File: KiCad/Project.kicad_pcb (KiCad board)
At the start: 2 copper layers, 70 x 40.6 mm, 46 parts, among them J2 Inputs Test Points, J3 Power & Output Test Points, Q1 BUK9832-55A, Q2 BUK9832-55A, SW1 Power, SW2 Fire, SW3 Freq Select, SW4 Fire Select, U1 TLV1117-50, U2 PIC16F1788-IP, U3 Audio Board

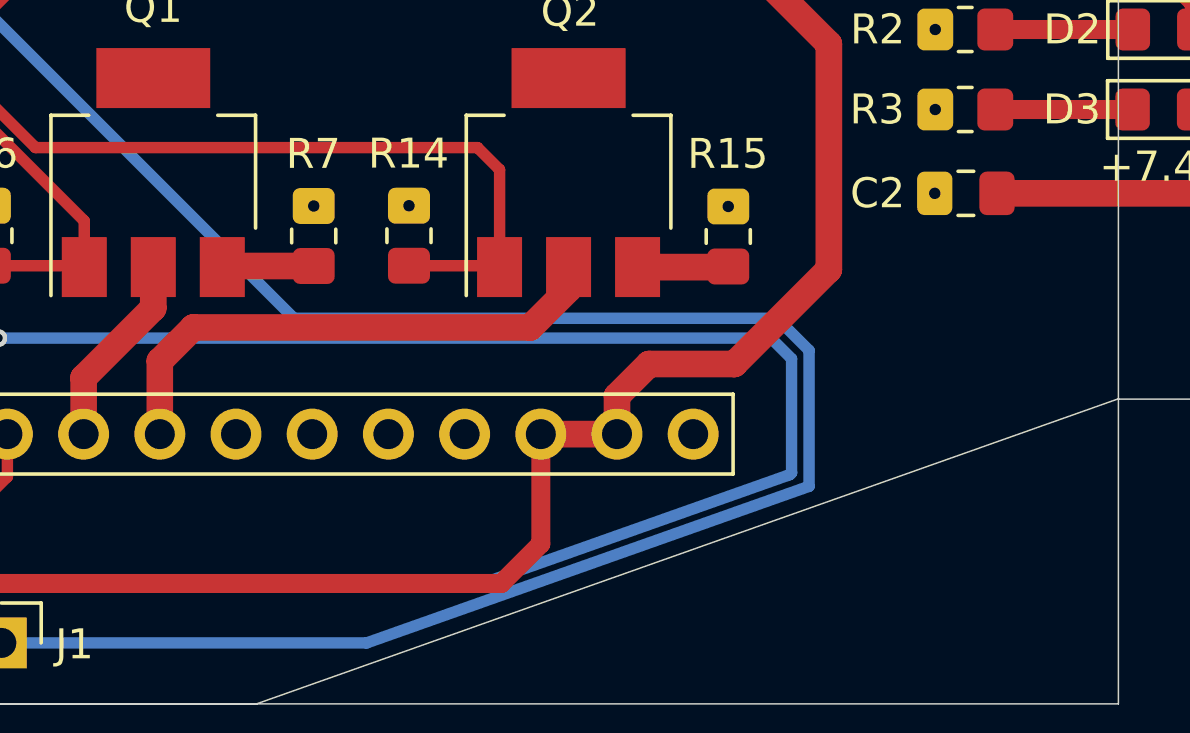
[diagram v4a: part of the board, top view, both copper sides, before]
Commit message: added title block and logo
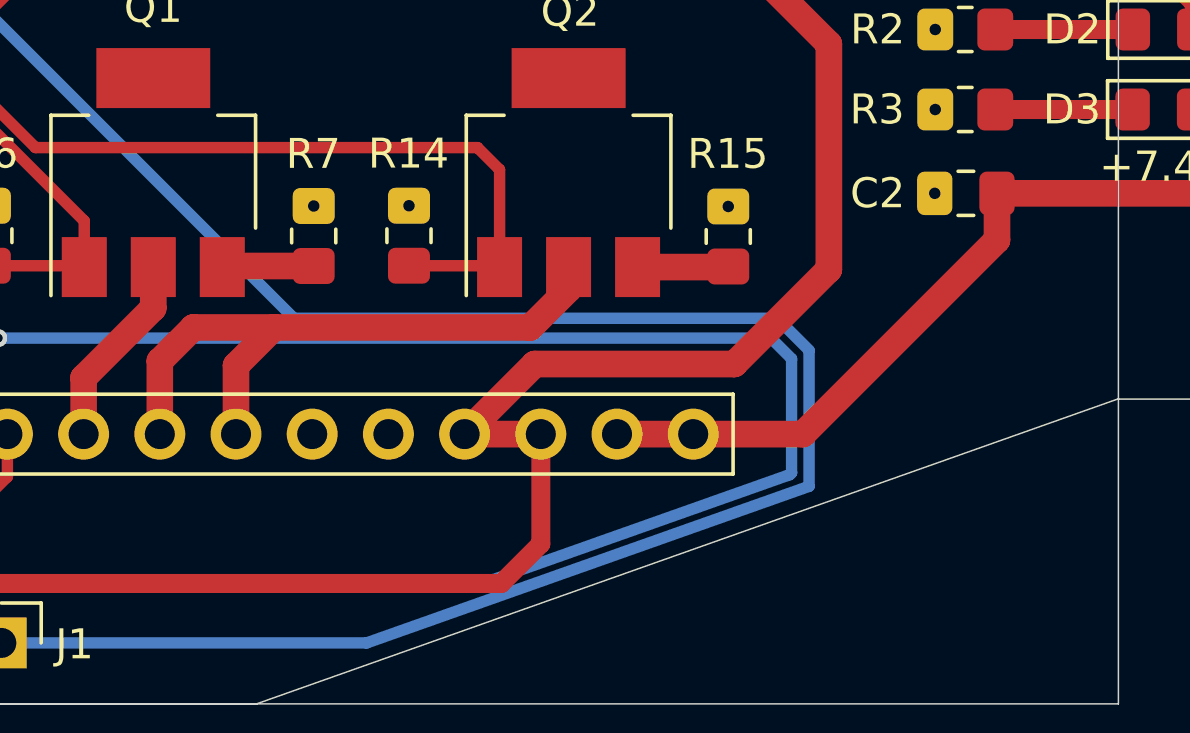
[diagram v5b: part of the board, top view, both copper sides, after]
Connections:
- REF** pad 10: (no net) -> GND
- REF** pad 12: GND -> +5V
- REF** pad 14: +5V -> Net-(D1-K)
- REF** pad 9: (no net) -> Net-(Q2-D)
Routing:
- net Net-(D1-K): track 77.0 -> 93.9 mm
- net +5V: track 143.8 -> 148.2 mm
- net Net-(Q2-D): track 22.4 -> 26.5 mm
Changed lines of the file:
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@@
 			(layers "*.Cu" "*.Mask")
 			(remove_unused_layers no)
+			(net 18 "Net-(Q2-D)")
 		)
 		(pad "10" thru_hole oval
@@
 			(layers "*.Cu" "*.Mask")
 			(remove_unused_layers no)
+			(net 2 "GND")
 		)
 		(pad "11" thru_hole oval
@@
 			(layers "*.Cu" "*.Mask")
 			(remove_unused_layers no)
-			(net 2 "GND")
+			(net 4 "+5V")
 		)
 		(pad "13" thru_hole oval
@@
 			(layers "*.Cu" "*.Mask")
 			(remove_unused_layers no)
-			(net 4 "+5V")
+			(net 3 "Net-(D1-K)")
 		)
 		(pad "15" thru_hole oval
@@
 	)
 	(segment
+		(start 144.188 44.2292)
+		(end 144.188 42.672)
+		(width 0.889)
+		(layer "F.Cu")
+		(net 3)
+	)
+	(segment
 		(start 136.144 31.505)
 		(end 143.9 31.505)
@@
 	)
 	(segment
+		(start 134.0612 50.6984)
+		(end 137.7188 50.6984)
+		(width 0.889)
+		(layer "F.Cu")
+		(net 3)
+	)
+	(segment
+		(start 137.7188 50.6984)
+		(end 144.188 44.2292)
+		(width 0.889)
+		(layer "F.Cu")
+		(net 3)
+	)
+	(segment
 		(start 152.146 42.672)
 		(end 155.067 39.751)
@@
 	)
 	(segment
+		(start 131.5212 50.6984)
+		(end 134.0612 50.6984)
+		(width 0.889)
+		(layer "F.Cu")
+		(net 3)
+	)
+	(segment
 		(start 144.188 42.672)
 		(end 152.146 42.672)
@@
 	)
 	(segment
-		(start 131.5212 50.6984)
-		(end 128.9812 50.6984)
+		(start 138.5824 45.212)
+		(end 138.5824 37.6936)
 		(width 0.889)
 		(layer "F.Cu")
@@
 	)
 	(segment
+		(start 128.778 48.3616)
+		(end 135.4328 48.3616)
+		(width 0.889)
+		(layer "F.Cu")
+		(net 4)
+	)
+	(segment
+		(start 138.5824 37.6936)
+		(end 134.1628 33.274)
+		(width 0.889)
+		(layer "F.Cu")
+		(net 4)
+	)
+	(segment
 		(start 134.1628 30.1244)
 		(end 134.8322 29.455)
@@
 	)
 	(segment
-		(start 138.5824 45.212)
-		(end 138.5824 37.6936)
-		(width 0.889)
-		(layer "F.Cu")
-		(net 4)
-	)
-	(segment
 		(start 134.498085 29.455)
 		(end 136.144 29.455)
@@
 	)
 	(segment
-		(start 131.5212 50.6984)
-		(end 131.5212 49.4284)
-		(width 0.889)
-		(layer "F.Cu")
-		(net 4)
-	)
-	(segment
 		(start 137.423 29.455)
 		(end 139.142 27.736)
@@
 	)
 	(segment
-		(start 134.8322 29.455)
-		(end 136.144 29.455)
-		(width 0.889)
-		(layer "F.Cu")
-		(net 4)
-	)
-	(segment
 		(start 142.353 35.292)
 		(end 142.748 35.687)
@@
 	)
 	(segment
-		(start 132.588 48.3616)
-		(end 135.4328 48.3616)
-		(width 0.889)
-		(layer "F.Cu")
-		(net 4)
-	)
-	(segment
 		(start 142.353 34.036)
 		(end 142.353 35.292)
@@
 	)
 	(segment
-		(start 128.9812 50.6984)
-		(end 128.9812 54.356)
-		(width 0.635)
-		(layer "F.Cu")
-		(net 4)
-	)
-	(segment
 		(start 127.6604 55.6768)
 		(end 109.2708 55.6768)
@@
 	)
 	(segment
-		(start 128.738085 23.695)
-		(end 134.498085 29.455)
-		(width 0.381)
+		(start 134.1628 33.274)
+		(end 134.1628 30.1244)
+		(width 0.889)
 		(layer "F.Cu")
 		(net 4)
 	)
 	(segment
-		(start 109.2708 55.6768)
-		(end 108.458 56.4896)
-		(width 0.635)
+		(start 134.8322 29.455)
+		(end 136.144 29.455)
+		(width 0.889)
 		(layer "F.Cu")
 		(net 4)
 	)
 	(segment
-		(start 138.5824 37.6936)
-		(end 134.1628 33.274)
-		(width 0.889)
+		(start 128.738085 23.695)
+		(end 134.498085 29.455)
+		(width 0.381)
 		(layer "F.Cu")
 		(net 4)
 	)
 	(segment
-		(start 135.4328 48.3616)
-		(end 138.5824 45.212)
-		(width 0.889)
+		(start 109.2708 55.6768)
+		(end 108.458 56.4896)
+		(width 0.635)
 		(layer "F.Cu")
 		(net 4)
 	)
 	(segment
-		(start 131.5212 49.4284)
-		(end 132.588 48.3616)
+		(start 126.4412 50.6984)
+		(end 128.9812 50.6984)
 		(width 0.889)
 		(layer "F.Cu")
@@
 	)
 	(segment
-		(start 134.1628 33.274)
-		(end 134.1628 30.1244)
+		(start 126.4412 50.6984)
+		(end 128.778 48.3616)
 		(width 0.889)
 		(layer "F.Cu")
@@
 	)
 	(segment
+		(start 135.4328 48.3616)
+		(end 138.5824 45.212)
+		(width 0.889)
+		(layer "F.Cu")
+		(net 4)
+	)
+	(segment
 		(start 151.003 30.48)
 		(end 148.259 27.736)
@@
 	)
 	(segment
+		(start 128.9812 54.356)
+		(end 128.9812 50.6984)
+		(width 0.635)
+		(layer "F.Cu")
+		(net 4)
+	)
+	(segment
 		(start 139.142 27.736)
 		(end 142.353 27.736)
@@
 	)
 	(segment
+		(start 118.8212 48.4124)
+		(end 120.0912 47.1424)
+		(width 0.889)
+		(layer "F.Cu")
+		(net 18)
+	)
+	(segment
 		(start 174.1424 68.7064)
 		(end 174.1424 64.1096)
@@
 	)
 	(segment
+		(start 118.8212 50.6984)
+		(end 118.8212 48.4124)
+		(width 0.889)
+		(layer "F.Cu")
+		(net 18)
+	)
+	(segment
 		(start 129.907 45.869)
 		(end 128.6336 47.1424)
@@
 	)
 	(segment
+		(start 128.6336 47.1424)
+		(end 120.0912 47.1424)
+		(width 0.889)
+		(layer "F.Cu")
+		(net 18)
+	)
+	(segment
 		(start 116.2812 48.26)
 		(end 116.2812 50.6984)
@@
 	)
 	(segment
-		(start 128.6336 47.1424)
+		(start 120.0912 47.1424)
 		(end 117.3988 47.1424)
 		(width 0.889)

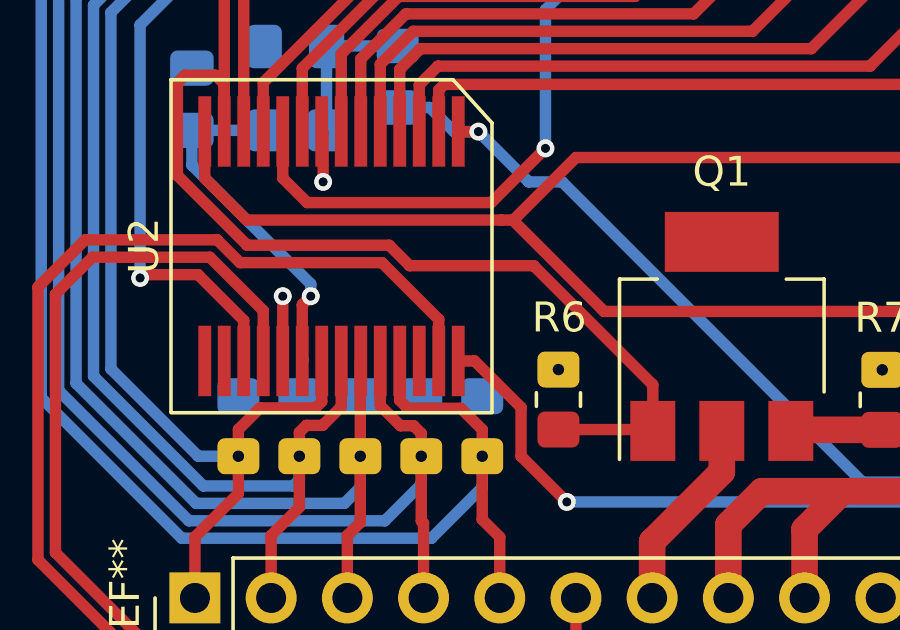
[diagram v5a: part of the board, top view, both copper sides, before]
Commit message: recovered some lost parts of the schematic, still needs a bit of work to get back
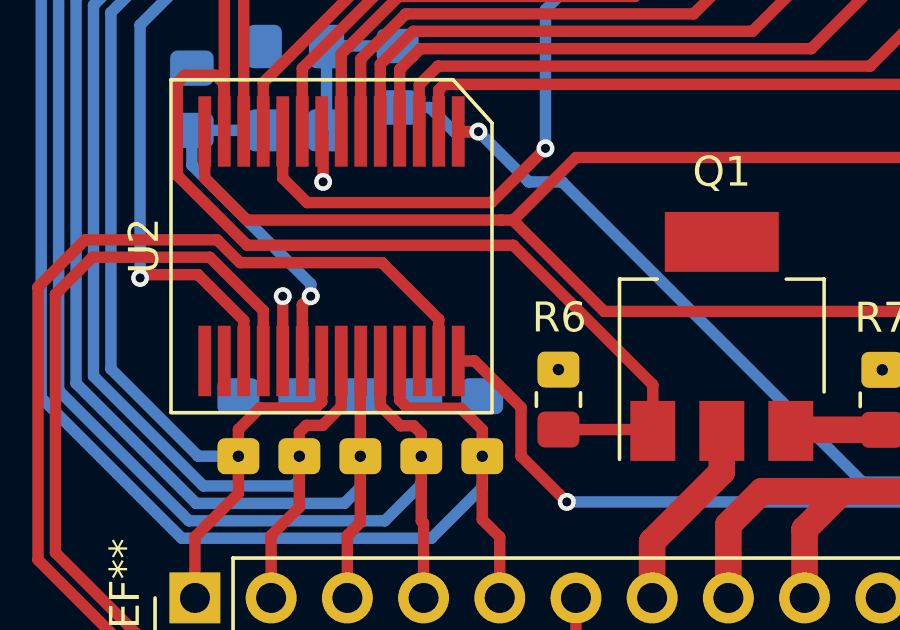
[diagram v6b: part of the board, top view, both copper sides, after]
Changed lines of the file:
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@@
-	)
-	(segment
-		(start 109.795 39.624)
-		(end 105.659 39.624)
-		(width 0.381)
-		(layer "F.Cu")
-		(net 16)
 	)
 	(segment
@@
 	)
 	(segment
-		(start 113.763 45.13)
-		(end 113.763 43.592)
+		(start 97.917 36.615658)
+		(end 97.917 33.528)
 		(width 0.381)
 		(layer "F.Cu")
@@
 	)
 	(segment
-		(start 104.9764 38.9414)
-		(end 100.242742 38.9414)
+		(start 97.917 33.528)
+		(end 98.171 33.274)
 		(width 0.381)
 		(layer "F.Cu")
@@
 	)
 	(segment
-		(start 98.171 33.274)
-		(end 99.187 33.274)
+		(start 99.822 21.0312)
+		(end 99.7712 21.082)
 		(width 0.381)
 		(layer "F.Cu")
@@
 	)
 	(segment
-		(start 99.822 21.0312)
-		(end 99.7712 21.082)
-		(width 0.381)
-		(layer "F.Cu")
-		(net 16)
-	)
-	(segment
-		(start 97.917 36.615658)
-		(end 97.917 33.528)
-		(width 0.381)
-		(layer "F.Cu")
-		(net 16)
-	)
-	(segment
-		(start 99.478 33.565)
-		(end 99.478 35.149)
-		(width 0.381)
-		(layer "F.Cu")
-		(net 16)
-	)
-	(segment
-		(start 97.917 33.528)
-		(end 98.171 33.274)
-		(width 0.381)
-		(layer "F.Cu")
-		(net 16)
-	)
-	(segment
-		(start 113.763 43.592)
-		(end 109.795 39.624)
-		(width 0.381)
-		(layer "F.Cu")
-		(net 16)
-	)
-	(segment
 		(start 113.718 45.085)
 		(end 113.763 45.13)
@@
 	)
 	(segment
-		(start 105.659 39.624)
-		(end 104.9764 38.9414)
+		(start 98.171 33.274)
+		(end 99.187 33.274)
 		(width 0.381)
 		(layer "F.Cu")
@@
 	)
 	(segment
+		(start 109.1124 38.9414)
+		(end 100.242742 38.9414)
+		(width 0.381)
+		(layer "F.Cu")
+		(net 16)
+	)
+	(segment
 		(start 99.478 27.817942)
 		(end 99.478 35.149)
 		(width 0.381)
+		(layer "F.Cu")
+		(net 16)
+	)
+	(segment
+		(start 113.763 43.592)
+		(end 109.1124 38.9414)
+		(width 0.381)
+		(layer "F.Cu")
+		(net 16)
+	)
+	(segment
+		(start 113.763 45.13)
+		(end 113.763 43.592)
+		(width 0.381)
+		(layer "F.Cu")
+		(net 16)
+	)
+	(segment
+		(start 99.478 33.565)
+		(end 99.478 35.149)
+		(width 0.381)

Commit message: fixed the schematics, and got the new components added into the PCB, need to rerun a lot of traces.
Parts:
- removed the R13 at (174.1, 70.3)
- added C7: 1uF, Capacitor_SMD:C_0805_2012Metric_Pad1.18x1.45mm_HandSolder, F.Cu at (205.4, 125.4)
- added J4: ~, Connector_PinHeader_2.54mm:PinHeader_1x11_P2.54mm_Vertical, F.Cu at (54.5, 64.1)
- added J5: ~, Connector_PinHeader_2.54mm:PinHeader_1x16_P2.54mm_Vertical, F.Cu at (49.8, 64.1)
- added J6: ~, Connector_PinHeader_2.54mm:PinHeader_1x11_P2.54mm_Vertical, F.Cu at (197.6, 85.7)
- added J7: ~, Connector_PinHeader_2.54mm:PinHeader_1x16_P2.54mm_Vertical, F.Cu at (193.0, 85.7)
- added LD2: Laser Diode, AlexWheelockFootprintLibrary:Project_Locking_Output_Header, F.Cu at (205.1, 94.0)
- added Q1: BUK9832-55A, Package_TO_SOT_SMD:SOT-223-3_TabPin2, F.Cu at (113.0, 106.5)
- added R12: 0Ω, Resistor_SMD:R_0805_2012Metric_Pad1.20x1.40mm_HandSolder, F.Cu at (105.0, 109.0)
- added R15: 1kΩ, Resistor_SMD:R_1206_3216Metric_Pad1.30x1.75mm_HandSolder, F.Cu at (185.0, 73.3)
- added R9: 100kΩ, Resistor_SMD:R_0805_2012Metric_Pad1.20x1.40mm_HandSolder, F.Cu at (105.0, 106.0)
- J2: value Inputs Test Points -> Power & Output Test Points; footprint Connector_PinHeader_2.54mm:PinHeader_1x05_P2.54mm_Vertical -> Connector_PinHeader_2.54mm:PinHeader_1x04_P2.54mm_Vertical
- J3: value Power & Output Test Points -> Inputs Test Points; footprint Connector_PinHeader_2.54mm:PinHeader_1x04_P2.54mm_Vertical -> Connector_PinHeader_2.54mm:PinHeader_1x05_P2.54mm_Vertical
- moved C8 64.6 mm to (205.4, 128.5)
- moved SW3 51.1 mm to (204.4, 116.1), turned to 0 degrees
- moved SW2 50.0 mm to (205.1, 106.9), turned to 0 degrees
- moved S1 49.4 mm to (205.1, 100.4), turned to 0 degrees
- moved LD1 47.1 mm to (205.1, 87.5), turned to 0 degrees
- moved U3 37.7 mm to (168.0, 91.7), turned to 0 degrees
- moved J2 37.1 mm to (88.6, 35.1), turned to 0 degrees
- moved SW4 35.9 mm to (199.2, 115.4)
- moved Q2 33.3 mm to (104.9, 73.3)
- moved Q3 33.3 mm to (118.8, 73.3)
- moved R4 33.3 mm to (88.8, 76.3)
- moved R6 33.3 mm to (92.9, 76.3)
- moved R7 33.3 mm to (94.9, 76.3)
- moved R8 33.3 mm to (96.9, 76.3)
- moved U2 33.3 mm to (91.9, 70.3)
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- renumbered C7 to C5, D3 to D1, D1 to D2, D2 to D3, Q1 to Q2, Q2 to Q3, R3 to R1, R6 to R10, R14 to R11, R7 to R13, R15 to R14, R5 to R3, R8 to R4, R9 to R5, R10 to R6, R11 to R7, R12 to R8
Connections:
- BT1 pad : GND -> (no net)
- C1 pad 1: Net-(D1-K) -> +7.4V
- C2 pad 1: Net-(D1-K) -> +7.4V
- C3 pad 1: +5V -> +5V_Top
- C4 pad 1: +5V -> +5V_Top
- C5 pad 2: GND -> Net-(C5-Pad2)
- C6 pad 1: GND -> Net-(C6-Pad1)
- C6 pad 2: +5V -> +5V_Top
- C8 pad 1: +5V -> +5V_Top
- C8 pad 2: Net-(U2-INT/AN12/RB0) -> Fire_Top
- D1 pad 1: Net-(D3-K) (its old number) -> Net-(D1-K)
- D1 pad 2: Net-(D1-K) -> +7.4V
- D2 pad 1: Net-(D1-K) -> +7.4V
- D2 pad 2: +5V -> +5V_Top
- D3 pad 2: +5V -> +5V_Top
- D5 pad 1: +7.4V -> +7.4V_Top
- J1 pad 2: +5V -> +5V_Top
- J1 pad 3: GND -> Net-(J1-Pad3)
- J2 pad 1: Net-(U2-INT/AN12/RB0) -> +7.4V
- J2 pad 2: Net-(SW3-A) -> +5V_Top
- J2 pad 3: Net-(U2-P1B/AN8/RB2) -> Laser/PWM
- J2 pad 4: Net-(U2-PGM/C12IN2-/AN8/RB3) -> Solenoid
- J3 pad 1: Net-(D1-K) -> Fire
- J3 pad 2: +5V -> Frequency Select
- J3 pad 3: Net-(Q2-G) -> Full-Auto
- J3 pad 4: Net-(Q1-G) -> Burst
- LD1 pad 1: +5V -> +5V_Top
- LD1 pad 2: Net-(LD1-K) -> Laser/PWM_Top
- Q2 pad 1: Net-(Q1-G) -> Net-(Q2-G)
- Q2 pad 2: Net-(LD1-K) -> Laser/PWM
- Q3 pad 1: Net-(Q2-G) -> Net-(Q3-G)
- Q3 pad 2: Net-(Q2-D) -> Solenoid
- R1 pad 2: Net-(D3-K) (its old number) -> Net-(D1-K)
- R10 pad 1: Net-(Q1-G) -> Net-(Q2-G)
- R10 pad 2: GND -> Net-(R10-Pad2)
- R11 pad 1: Net-(Q2-G) -> Net-(Q3-G)
- R11 pad 2: GND -> Net-(R11-Pad2)
- R13 pad 2: GND -> Net-(R13-Pad2)
- R14 pad 2: GND -> Net-(R14-Pad2)
- R3 pad 2: +5V -> +5V_Top
- R4 pad 1: Net-(U2-INT/AN12/RB0) -> Fire
- R4 pad 2: GND -> Net-(R4-Pad2)
- R5 pad 1: Net-(SW3-A) -> Frequency Select
- R5 pad 2: GND -> Net-(R4-Pad2)
- R6 pad 1: Net-(U2-P1B/AN8/RB2) -> Full-Auto
- R6 pad 2: GND -> Net-(R4-Pad2)
- R7 pad 1: Net-(U2-PGM/C12IN2-/AN8/RB3) -> Burst
- R7 pad 2: GND -> Net-(R4-Pad2)
- R8 pad 1: Net-(U2-P1D/AN11/RB4) -> Semi-Auto
- R8 pad 2: GND -> Net-(R4-Pad2)
- S1 pad 1: +7.4V -> +7.4V_Top
- S1 pad 2: Net-(Q2-D) -> Solenoid_Top
- SW1 pad 2: Net-(D1-K) -> +7.4V_Top
- SW2 pad 1: +5V -> +5V_Top
- SW2 pad 2: Net-(U2-INT/AN12/RB0) -> Fire_Top
- SW3 pad 1: Net-(SW3-A) -> Frequency Select_Top
- SW3 pad 2: +5V -> +5V_Top
- SW4 pad 1: Net-(U2-PGM/C12IN2-/AN8/RB3) -> Burst_Top
- SW4 pad 2: Net-(U2-P1D/AN11/RB4) -> Semi-Auto_Top
- SW4 pad 3: +5V -> +5V_Top
- SW4 pad 4: +5V -> +5V_Top
- SW4 pad 5: Net-(U2-P1B/AN8/RB2) -> Full-Auto_Top
- U1 pad 2: +5V -> +5V_Top
- U1 pad 3: Net-(D1-K) -> +7.4V
- U2 pad 12: TRIG9 -> Net-(Q1-G)
- U2 pad 13: Net-(Q1-G) -> Net-(Q2-G)
- U2 pad 14: Net-(Q2-G) -> Net-(Q3-G)
- U2 pad 16: unconnected-(U2-RC5/SDO-Pad16) -> TRIG9
- U2 pad 2: TRIG0 -> unconnected-(U2-ULPWU/C12IN0-/AN0/RA0-Pad2)
- U2 pad 20: +5V -> +5V_Top
- U2 pad 21: Net-(U2-INT/AN12/RB0) -> Fire
- U2 pad 22: Net-(SW3-A) -> Frequency Select
- U2 pad 23: Net-(U2-P1B/AN8/RB2) -> Full-Auto
- U2 pad 24: Net-(U2-PGM/C12IN2-/AN8/RB3) -> Burst
- U2 pad 25: Net-(U2-P1D/AN11/RB4) -> Semi-Auto
- U3 pad 10: TRIG8 -> TRIG8_Top
- U3 pad 11: TRIG9 -> TRIG9_Top
- U3 pad 12: TRIG10 -> TRIG10_Top
- U3 pad 14: GND -> Net-(U3-GND-Pad14)
- U3 pad 15: GND -> Net-(U3-GND-Pad14)
- U3 pad 18: GND -> Net-(U3-GND-Pad14)
- U3 pad 2: TRIG0 -> TRIG0_Top
- U3 pad 21: VOL+ -> VOL+_Top
- U3 pad 27: GND -> Net-(U3-GND-Pad14)
- U3 pad 28: +5V -> +5V_Top
- U3 pad 3: TRIG1 -> TRIG1_Top
- U3 pad 4: TRIG2 -> TRIG2_Top
- U3 pad 5: TRIG3 -> TRIG3_Top
- U3 pad 6: TRIG4 -> TRIG4_Top
- U3 pad 7: TRIG5 -> TRIG5_Top
- U3 pad 8: TRIG6 -> TRIG6_Top
- U3 pad 9: TRIG7 -> TRIG7_Top
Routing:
- net Net-(Q3-G): track 0.00 -> 101.8 mm
- net Net-(Q2-G): track 101.8 -> 44.2 mm
- net Net-(Q1-G): track 44.2 -> 0.00 mm
- net +5V: track 148.2 -> 119.6 mm, vias 1 -> 0
- net +5V_Top: track 0.00 -> 23.4 mm, vias 0 -> 1
- net +7.4V: track 5.64 -> 0.00 mm
- net Net-(U2-INT/AN12/RB0): track 65.3 -> 60.5 mm
- net Net-(Q2-D): track 26.5 -> 21.9 mm
- net Net-(D3-K) (its old number): track 4.59 -> 0.00 mm
- net Net-(D1-K): track 93.9 -> 98.5 mm
- net Net-(D5-A): track 2.50 -> 0.00 mm
- net (no net): vias 1 -> 0

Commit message: PCB nearly done for the blaster
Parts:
- removed the REF** at (87.4, 82.0)
- removed the REF** at (91.7, 59.6)
- J2: footprint Connector_PinHeader_2.54mm:PinHeader_1x04_P2.54mm_Vertical -> Connector_PinHeader_2.54mm:PinHeader_1x05_P2.54mm_Vertical
- Q1, R12, R9: moved to B.Cu
- moved LD1 188.4 mm to (20.1, 52.1)
- moved LD2 183.3 mm to (26.7, 52.1)
- moved S1 176.4 mm to (34.8, 54.6), turned to 180 degrees
- moved J6 170.4 mm to (29.3, 59.5), turned to 90 degrees
- moved C8 169.1 mm to (53.8, 53.3), turned to -90 degrees
- moved J7 168.1 mm to (24.9, 81.9), turned to 90 degrees
- moved SW2 165.8 mm to (48.6, 52.1)
- moved SW3 149.8 mm to (67.7, 54.7), turned to 90 degrees
- moved C7 145.9 mm to (64.0, 89.5), turned to 180 degrees
- moved R15 145.6 mm to (41.0, 51.7), turned to 0 degrees
- moved D5 134.2 mm to (41.0, 55.2)
- moved SW4 134.1 mm to (71.6, 74.0)
- moved SW1 129.4 mm to (59.9, 54.6), turned to 180 degrees
- moved BT1 125.7 mm to (75.5, 62.6), turned to -90 degrees
- moved U3 110.4 mm to (59.9, 69.2), turned to -90 degrees
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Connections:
- C3 pad 1: +5V_Top -> +5V
- C4 pad 1: +5V_Top -> +5V
- C5 pad 2: Net-(C5-Pad2) -> GND
- C6 pad 1: Net-(C6-Pad1) -> GND
- C6 pad 2: +5V_Top -> +5V
- C7 pad 1: Net-(C7-Pad1) -> GND
- D2 pad 2: +5V_Top -> +5V
- D3 pad 2: +5V_Top -> +5V
- J1 pad 2: +5V_Top -> +5V
- J1 pad 3: Net-(J1-Pad3) -> GND
- J2 pad 2: +5V_Top -> +5V
- J2 pad 3: Laser/PWM -> Net-(Q3-G)
- J2 pad 4: Solenoid -> Net-(Q1-G)
- J5 pad 11: Net-(J5-Pad11) -> GND
- J5 pad 12: Net-(J5-Pad11) -> GND
- J5 pad 13: +5V_Top -> +5V
- J5 pad 14: +5V_Top -> +5V
- J7 pad 11: Net-(J7-Pad11) -> GND
- J7 pad 12: Net-(J7-Pad11) -> GND
- R10 pad 2: Net-(R10-Pad2) -> GND
- R11 pad 2: Net-(R11-Pad2) -> GND
- R12 pad 2: Net-(R12-Pad2) -> GND
- R13 pad 2: Net-(R13-Pad2) -> GND
- R14 pad 2: Net-(R14-Pad2) -> GND
- R3 pad 2: +5V_Top -> +5V
- R4 pad 2: Net-(R4-Pad2) -> GND
- R5 pad 2: Net-(R4-Pad2) -> GND
- R6 pad 2: Net-(R4-Pad2) -> GND
- R7 pad 2: Net-(R4-Pad2) -> GND
- R8 pad 2: Net-(R4-Pad2) -> GND
- R9 pad 2: Net-(R9-Pad2) -> GND
- U1 pad 2: +5V_Top -> +5V
- U2 pad 20: +5V_Top -> +5V
- U3 pad 14: Net-(U3-GND-Pad14) -> GND
- U3 pad 15: Net-(U3-GND-Pad14) -> GND
- U3 pad 18: Net-(U3-GND-Pad14) -> GND
- U3 pad 27: Net-(U3-GND-Pad14) -> GND
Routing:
- net Net-(D1-K): track 98.5 -> 4.59 mm, vias 1 -> 0
- net +7.4V: track 0.00 -> 88.6 mm, vias 0 -> 1
- net Frequency Select_Top: track 0.00 -> 74.8 mm, vias 0 -> 3
- net +5V_Top: track 23.4 -> 97.7 mm, vias 1 -> 0
- net Semi-Auto: track 0.00 -> 71.0 mm
- net +7.4V_Top: track 0.00 -> 70.3 mm
- net Burst: track 0.00 -> 67.9 mm
- net Net-(U2-P1D/AN11/RB4): track 66.4 -> 0.00 mm
- net Full-Auto: track 0.00 -> 65.9 mm
- net Frequency Select: track 0.00 -> 65.4 mm
- net Fire: track 0.00 -> 64.8 mm
- net Net-(U2-PGM/C12IN2-/AN8/RB3): track 63.7 -> 0.00 mm
- net Net-(U2-P1B/AN8/RB2): track 61.7 -> 0.00 mm
- net Net-(SW3-A): track 61.2 -> 0.00 mm
- net Net-(U2-INT/AN12/RB0): track 60.5 -> 0.00 mm
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- added copper zone on B.Cu, net GND
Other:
- board size 70 x 40.6 mm -> 129.7 x 40.6 mm
- board text added: "Laser2"
- board text added: "RST"
